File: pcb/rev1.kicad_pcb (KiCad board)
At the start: 2 copper layers, 99.9 x 99.9 mm, 50 parts, among them SW1 SW_Push, SW10 SW_Push, SW11 SW_Push, SW12 SW_Push, SW13 SW_Push, SW14 SW_Push, SW15 SW_Push, SW16 SW_Push, SW2 SW_Push, SW3 SW_Push, SW4 SW_Push, SW5 SW_Push, SW6 SW_Push, SW7 SW_Push, SW8 SW_Push, SW9 SW_Push, U1 XIAO-RP2040-DIP, U2 OLED_0.91_128x32

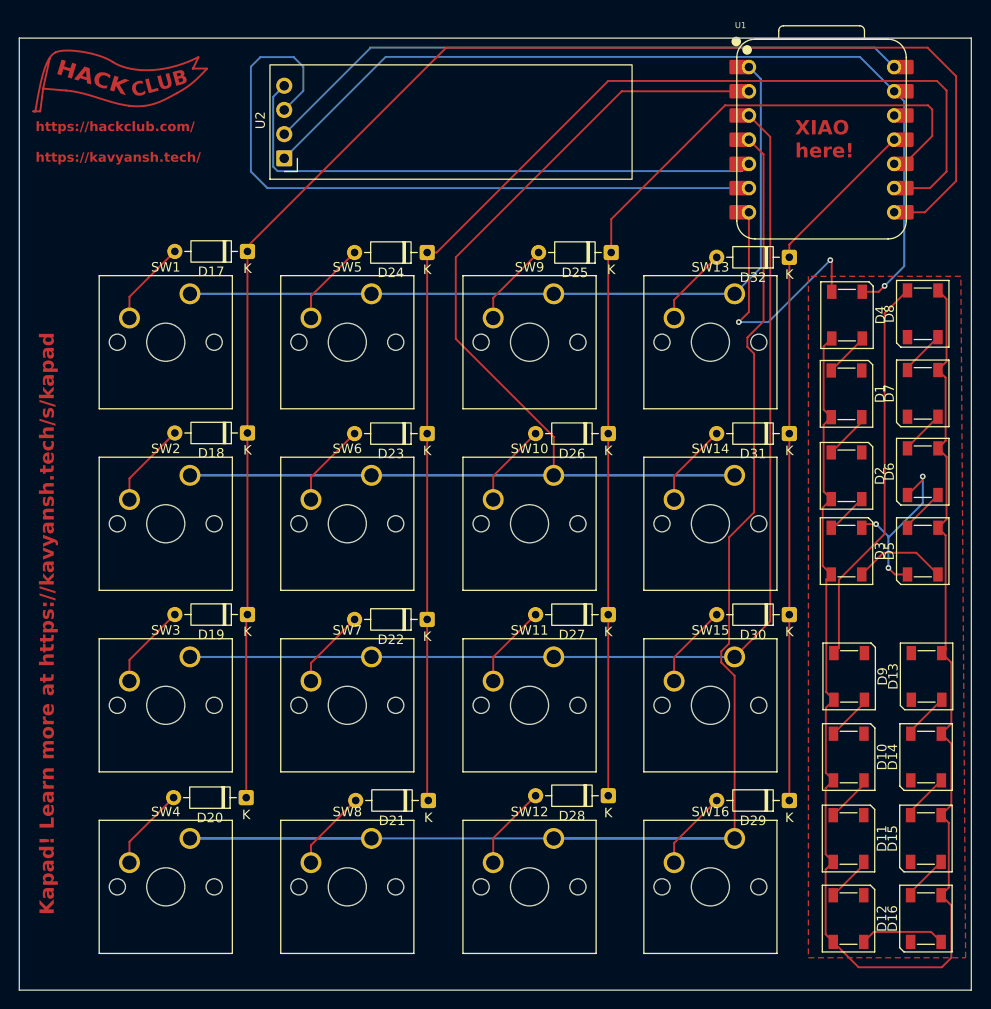
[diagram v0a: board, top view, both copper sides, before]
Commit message: Fixed LED footprint
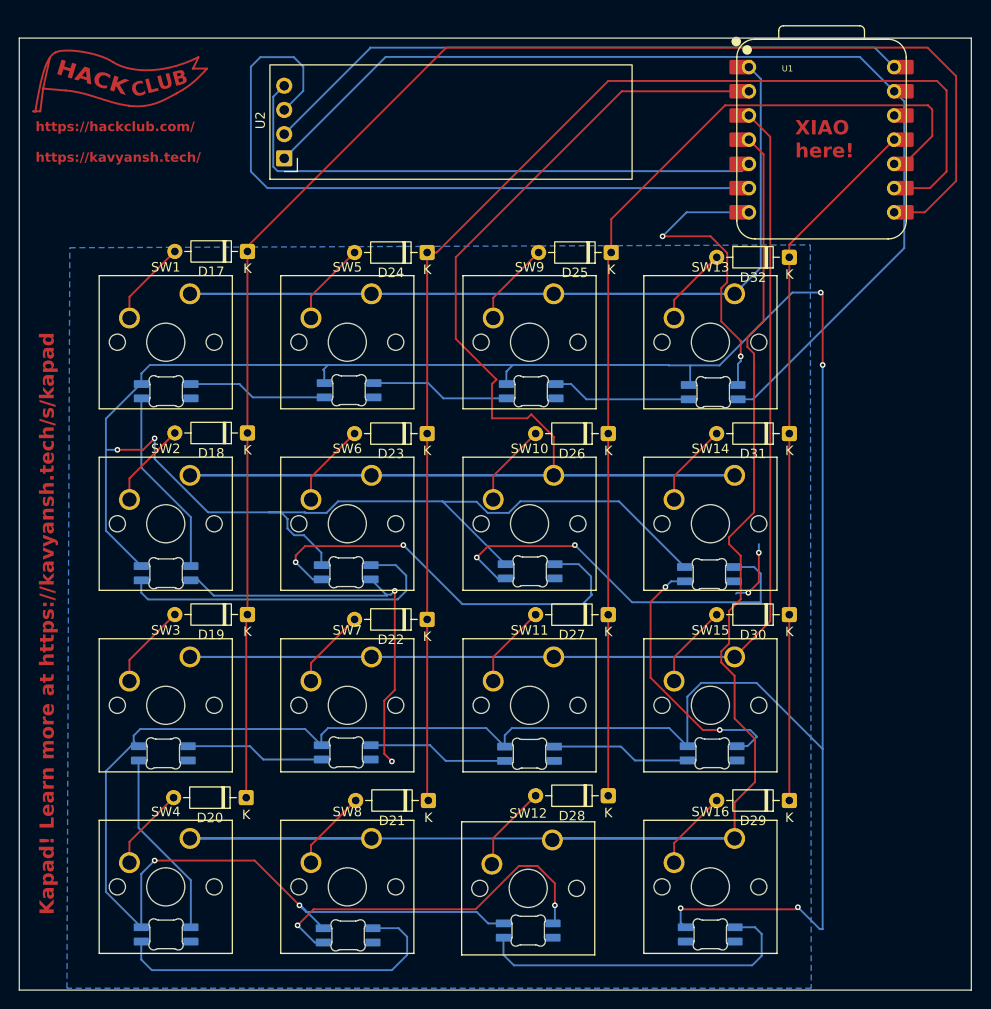
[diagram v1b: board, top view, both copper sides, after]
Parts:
- D1, D10, D11, D12, D13, D14, D15, D16, D2, D3, D4, D5, D6, D7, D8, D9: footprint LED_SMD:LED_SK6812_PLCC4_5.0x5.0mm_P3.2mm -> Hackclub symbols:MX_SK6812MINI-E_REV
- moved D16 79.8 mm to (169.1, 119.0), turned to 0 degrees
- moved D5 79.4 mm to (169.1, 81.1), turned to 0 degrees
- moved D12 75.3 mm to (168.8, 100.0), turned to 0 degrees
- moved D3 74.7 mm to (169.1, 62.0), turned to 0 degrees
- moved D15 60.8 mm to (188.2, 119.1), turned to 0 degrees
- moved D6 60.7 mm to (188.0, 81.0), turned to 0 degrees
- moved D11 54.6 mm to (188.0, 99.9), turned to 0 degrees
- moved D2 54.1 mm to (188.3, 61.9), turned to 0 degrees
- moved D14 43.8 mm to (207.1, 118.6), turned to 0 degrees
- moved D7 43.4 mm to (207.3, 80.9), turned to 0 degrees
- moved D10 33.9 mm to (207.2, 100.0), turned to 0 degrees
- moved D1 33.5 mm to (207.4, 62.0), turned to 0 degrees
- moved D13 31.6 mm to (226.2, 119.0), turned to 0 degrees
- moved D8 31.6 mm to (226.1, 81.2), turned to 0 degrees
- moved D9 14.7 mm to (226.4, 100.0), turned to 0 degrees
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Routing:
- net +5V: track 157.4 -> 439.0 mm, vias 0 -> 8
- net GND: track 113.8 -> 161.1 mm
- net Net-(D6-DOUT): track 4.65 -> 45.0 mm, vias 0 -> 2
- net Net-(D7-DOUT): track 4.78 -> 42.8 mm, vias 0 -> 2
- net Net-(D14-DIN): track 4.98 -> 38.1 mm, vias 0 -> 2
- net Net-(D15-DIN): track 4.83 -> 36.8 mm
- net Net-(D5-DOUT): track 4.76 -> 35.5 mm
- net Net-(D13-DIN): track 4.91 -> 35.2 mm
- net Net-(D8-DOUT): track 41.2 -> 28.7 mm, vias 0 -> 2
- net Net-(D12-DOUT): track 8.99 -> 19.8 mm
- net Net-(D2-DOUT): track 4.44 -> 14.6 mm
- net Net-(D3-DOUT): track 9.89 -> 19.7 mm
- net Net-(D1-DIN): track 4.71 -> 14.6 mm
- net Net-(D11-DOUT): track 4.83 -> 14.6 mm
- net Net-(D10-DOUT): track 4.98 -> 14.7 mm
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- added copper zone on B.Cu, net GND
- removed copper zone on F.Cu, net GND

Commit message: Fixed LEDs not getting power
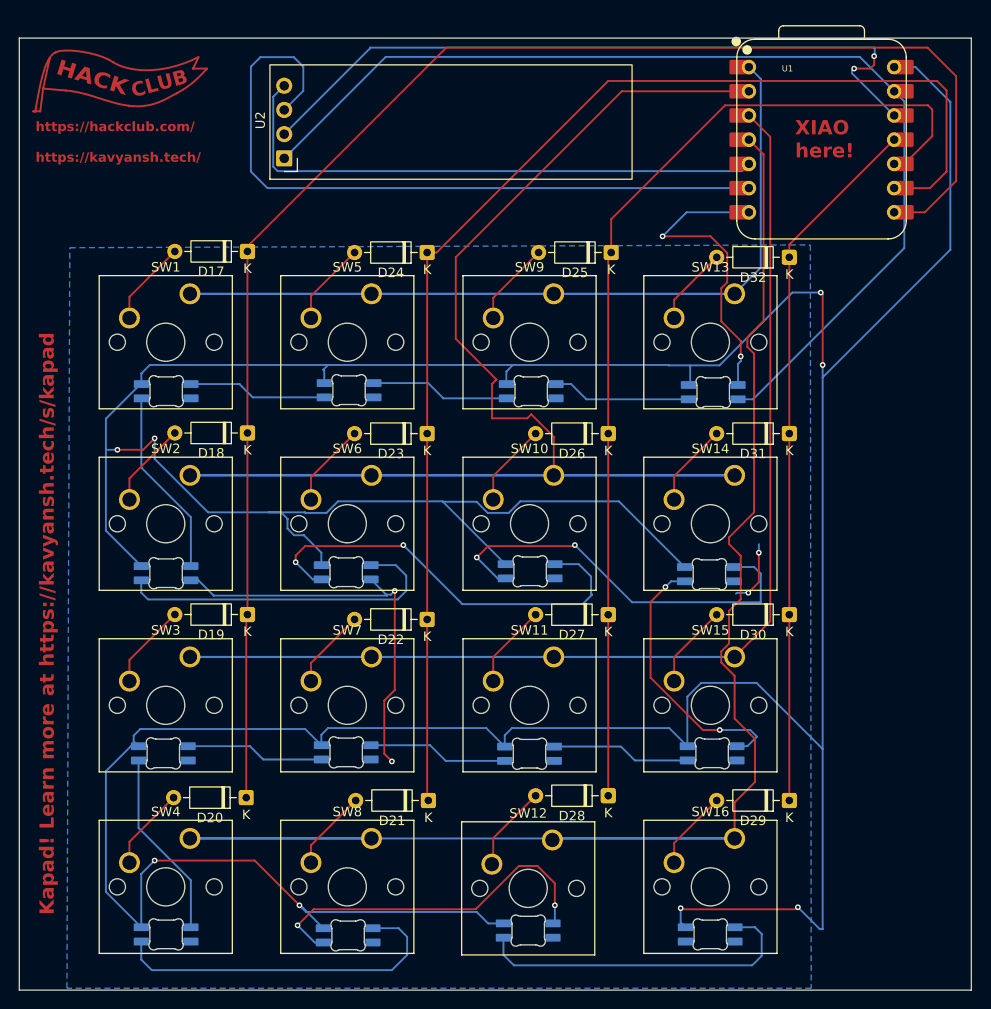
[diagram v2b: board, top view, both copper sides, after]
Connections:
- U1 pad 12: unconnected-(U1-3V3-Pad12) -> VCC
- U1 pad 14: VCC -> +5V
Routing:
- net +5V: track 439.0 -> 480.8 mm
- net VCC: track 68.7 -> 76.8 mm, vias 0 -> 2
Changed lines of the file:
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@@
 	(net 44 "Net-(U1-GPIO7{slash}SCL)")
 	(net 45 "Net-(U1-GPIO6{slash}SDA)")
-	(net 46 "unconnected-(U1-3V3-Pad12)")
-	(net 47 "VCC")
+	(net 46 "VCC")
 	(footprint "Hackclub symbols:MX_SK6812MINI-E_REV"
 		(layer "F.Cu")
@@
 			(layers "*.Cu" "*.Mask")
 			(remove_unused_layers no)
-			(net 47 "VCC")
+			(net 46 "VCC")
 			(pinfunction "VCC")
 			(pintype "power_in")
@@
 			(layers "*.Cu" "*.Mask")
 			(remove_unused_layers no)
-			(net 46 "unconnected-(U1-3V3-Pad12)")
+			(net 46 "VCC")
 			(pinfunction "3V3")
 			(pintype "passive")
@@
 			(layers "F.Cu" "F.Mask")
 			(roundrect_rratio 0.1)
-			(net 46 "unconnected-(U1-3V3-Pad12)")
+			(net 46 "VCC")
 			(pinfunction "3V3")
 			(pintype "passive")
@@
 			(layers "*.Cu" "*.Mask")
 			(remove_unused_layers no)
-			(net 47 "VCC")
+			(net 4 "+5V")
 			(pinfunction "VBUS")
 			(pintype "passive")
@@
 			(layers "F.Cu" "F.Mask")
 			(roundrect_rratio 0.1)
-			(net 47 "VCC")
+			(net 4 "+5V")
 			(pinfunction "VBUS")
 			(pintype "passive")
@@
 	)
 	(segment
+		(start 251.4 36.7)
+		(end 247.74 33.04)
+		(width 0.2)
+		(layer "B.Cu")
+		(net 4)
+	)
+	(segment
 		(start 166.5125 66.3025)
 		(end 166.422586 66.3025)
@@
 	)
 	(segment
+		(start 251.4 52.2)
+		(end 251.4 36.7)
+		(width 0.2)
+		(layer "B.Cu")
+		(net 4)
+	)
+	(segment
 		(start 235.4 121.2)
 		(end 237.7 123.5)
@@
 	)
 	(segment
+		(start 238 64.3)
+		(end 238 65.6)
+		(width 0.2)
+		(layer "B.Cu")
+		(net 4)
+	)
+	(segment
 		(start 221.855 64.345)
 		(end 227.16778 64.345)
@@
 	)
 	(segment
+		(start 247.74 33.04)
+		(end 245.5 33.04)
+		(width 0.2)
+		(layer "B.Cu")
+		(net 4)
+	)
+	(segment
 		(start 227.16778 64.345)
 		(end 234.81278 56.7)
@@
 	)
 	(segment
-		(start 238 64.3)
+		(start 238 65.6)
+		(end 251.4 52.2)
+		(width 0.2)
+		(layer "B.Cu")
+		(net 4)
+	)
+	(segment
+		(start 238 65.6)
 		(end 238 104.6)
 		(width 0.2)
@@
 	)
 	(segment
-		(start 190.5 31.08)
-		(end 190.5 31)
+		(start 243 33.2)
+		(end 243.4 32.8)
+		(width 0.2)
+		(layer "F.Cu")
+		(net 46)
+	)
+	(segment
+		(start 243.4 32.8)
+		(end 243.4 31.9)
+		(width 0.2)
+		(layer "F.Cu")
+		(net 46)
+	)
+	(segment
+		(start 241.3 33.2)
+		(end 243 33.2)
+		(width 0.2)
+		(layer "F.Cu")
+		(net 46)
+	)
+	(via
+		(at 243.4 31.9)
+		(size 0.6)
+		(drill 0.3)
+		(layers "F.Cu" "B.Cu")
+		(net 46)
+	)
+	(via
+		(at 241.3 33.2)
+		(size 0.6)
+		(drill 0.3)
+		(layers "F.Cu" "B.Cu")
+		(net 46)
+	)
+	(segment
+		(start 243.4 31.9)
+		(end 243.4 31.72)
+		(width 0.2)
+		(layer "B.Cu")
+		(net 46)
+	)
+	(segment
+		(start 243.46 31.66)
+		(end 243.46 31)
 		(width 0.2)
 		(layer "B.Cu")
-		(net 47)
+		(net 46)
+	)
+	(segment
+		(start 241.08 33.7)
+		(end 245.5 38.12)
+		(width 0.2)
+		(layer "B.Cu")
+		(net 46)
+	)
+	(segment
+		(start 241.3 33.2)
+		(end 241.08 33.42)
+		(width 0.2)
+		(layer "B.Cu")
+		(net 46)
 	)
 	(segment
 		(start 243.46 31)
-		(end 245.5 33.04)
+		(end 190.5 31)
 		(width 0.2)
 		(layer "B.Cu")
-		(net 47)
+		(net 46)
 	)
 	(segment
 		(start 190.5 31)
-		(end 243.46 31)
+		(end 190.5 31.08)
 		(width 0.2)
 		(layer "B.Cu")
-		(net 47)
+		(net 46)
 	)
 	(segment
-		(start 181.5 40.08)
-		(end 190.5 31.08)
+		(start 243.4 31.72)
+		(end 243.46 31.66)
+		(width 0.2)
+		(layer "B.Cu")
+		(net 46)
+	)
+	(segment
+		(start 190.5 31.08)
+		(end 181.5 40.08)
+		(width 0.2)
+		(layer "B.Cu")
+		(net 46)
+	)
+	(segment
+		(start 241.08 33.42)
+		(end 241.08 33.7)
 		(width 0.2)
 		(layer "B.Cu")
-		(net 47)
+		(net 46)
 	)
 	(segment
@@
 		(width 0.2)
 		(layer "B.Cu")
-		(net 47)
+		(net 46)
 	)
 	(zone
